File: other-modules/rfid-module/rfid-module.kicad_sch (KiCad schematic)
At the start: 69 parts, among them IC1 MCP23017-E_SO, IC2 TPS61040DBVR, Q1 BSS138, Q2 BSS138

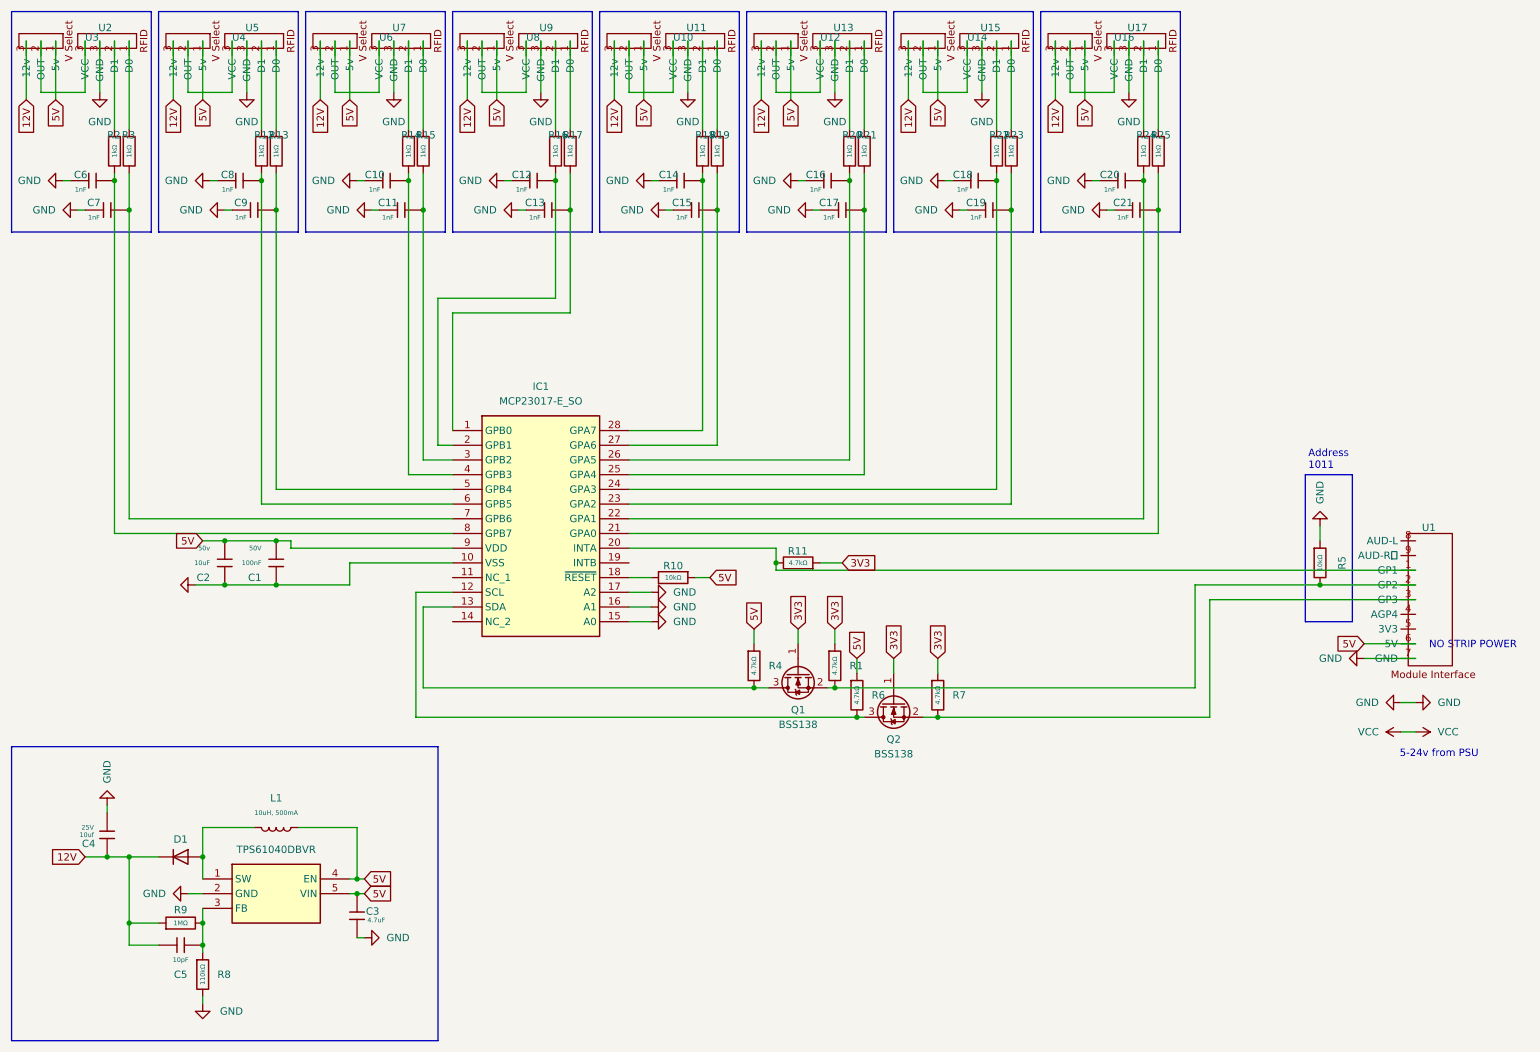
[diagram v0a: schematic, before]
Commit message: finish relay + start rfid
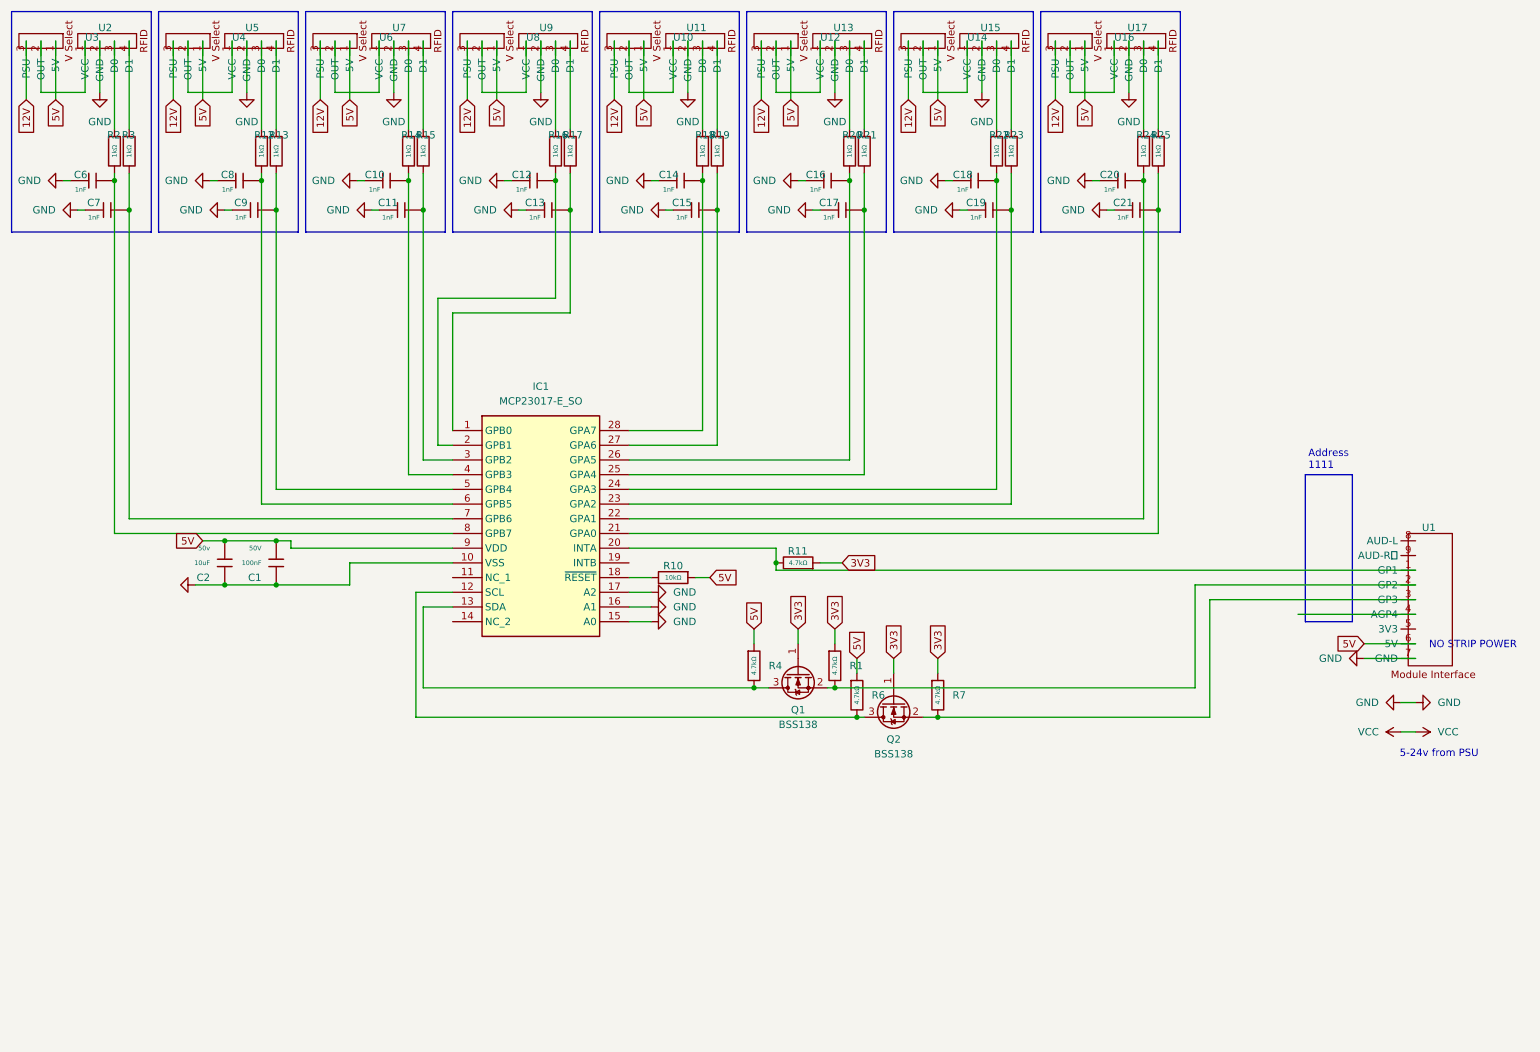
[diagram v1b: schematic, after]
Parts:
- removed C3: 4.7uF, PCM_JLCPCB:C_0402, symbol PCM_JLCPCB-Capacitors:0402,4.7uF
- removed C4: 10uf, PCM_JLCPCB:C_0402, symbol PCM_JLCPCB-Capacitors:0402,1uF
- removed C5: 10pF, PCM_JLCPCB:C_0402, symbol PCM_JLCPCB-Capacitors:0402,10pF
- removed D1: 1N4148WT, symbol Diode:1N4148WT
- removed IC2: TPS61040DBVR, symbol TPS61040:TPS61040DBVR
- removed L1: 10uH, 500mA, PCM_JLCPCB:L_0603, symbol PCM_JLCPCB-Inductors:10uH,3mA
- removed R5: 10kΩ, PCM_JLCPCB:R_0402, symbol PCM_JLCPCB-Resistors:0402,10kΩ
- removed R8: 110kΩ, PCM_JLCPCB:R_0402, symbol PCM_JLCPCB-Resistors:0402,1MΩ
- removed R9: 1MΩ, PCM_JLCPCB:R_0402, symbol PCM_JLCPCB-Resistors:0402,1MΩ
- C1, C10, C11, C12, C13, C14, C15, C16, C17, C18, C19, C2, C20, C21, C6, C7, C8, C9: footprint PCM_JLCPCB:C_0402 -> Capacitor_SMD:C_0603_1608Metric_Pad1.08x0.95mm_HandSolder
- IC1: footprint (none) -> Imported:MCP23017
- R1, R10, R11, R12, R13, R14, R15, R16, R17, R18, R19, R2, R20, R21, R22, R23, R24, R25, R3, R4, R6, R7: footprint PCM_JLCPCB:R_0402 -> Resistor_SMD:R_0603_1608Metric_Pad0.98x0.95mm_HandSolder
- U10, U12, U14, U16, U3, U4, U6, U8: footprint (none) -> ProjectDMX:RFID PSU Select
- U11, U13, U15, U17, U2, U5, U7, U9: footprint (none) -> ProjectDMX:RFID JST
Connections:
- net GND: now also U11.2 (GND), U13.2 (GND), U15.2 (GND), U17.2 (GND), U2.2 (GND), U5.2 (GND), U7.2 (GND), U9.2 (GND); no longer U11.3 (VCC), U13.3 (VCC), U15.3 (VCC), U17.3 (VCC), U2.3 (VCC), U5.3 (VCC), U7.3 (VCC), U9.3 (VCC)
- net at R22.1: now also U15.3 (D0); no longer U15.2 (D1)
- net at R13.1: now also U5.4 (D1); no longer U5.1 (D0)
- net at U16.2 (OUT): now also U17.1 (VCC); no longer U17.3 (VCC)
- net at R25.1: now also U17.4 (D1); no longer U17.1 (D0)
- net at U14.2 (OUT): now also U15.1 (VCC); no longer U15.3 (VCC)
- net at U9.1 (VCC): now also U8.2 (OUT); no longer R17.1
- net at R16.1: now also U9.3 (D0); no longer U9.2 (D1)
- net at R24.1: now also U17.3 (D0); no longer U17.2 (D1)
- net at U13.1 (VCC): now also U12.2 (OUT); no longer R21.1
- net at R20.1: now also U13.3 (D0); no longer U13.2 (D1)
- net at U7.1 (VCC): now also U6.2 (OUT); no longer R15.1
- net at R14.1: now also U7.3 (D0); no longer U7.2 (D1)
- net at U10.2 (OUT): now also U11.1 (VCC); no longer U11.3 (VCC)
- net at U2.1 (VCC): now also U3.2 (OUT); no longer R3.1
- net at R2.1: now also U2.3 (D0); no longer U2.2 (D1)
- net at R23.1: now also U15.4 (D1); no longer U15.1 (D0)
- net at R19.1: now also U11.4 (D1); no longer U11.1 (D0)
- net at R18.1: now also U11.3 (D0); no longer U11.2 (D1)
- net at R12.1: now also U5.3 (D0); no longer U5.2 (D1)
- net at U4.2 (OUT): now also U5.1 (VCC); no longer U5.3 (VCC)
- new net: R17.1, U9.4 (D1)
- new net: R21.1, U13.4 (D1)
- new net: R15.1, U7.4 (D1)
- new net: R3.1, U2.4 (D1)
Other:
- note added: "Address 1111"
- note removed: "Address 1011"
